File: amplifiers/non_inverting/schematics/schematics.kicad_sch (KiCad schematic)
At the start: 5 parts, among them J1 15V, U1 LM741

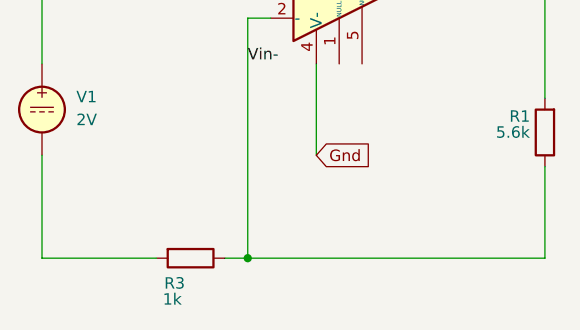
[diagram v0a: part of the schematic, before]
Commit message: docs: reorganize non-inverting amplifier schematics and add documentation
Completes documentation for the non-inverting amplifier circuit using
the LM741 operational amplifier. The schematics have been moved from
the LM741 directory to a dedicated non-inverting amplifier directory.

Only specific measurements for the LM741 will be foubd under the LM741
directory going forward.

Breaking changes: None

Resolves: None
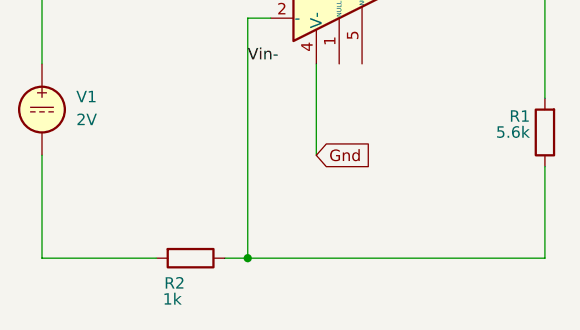
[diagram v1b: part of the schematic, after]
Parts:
- renumbered R3 to R2
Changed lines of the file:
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@@
 		(on_board yes)
 		(dnp no)
-		(property "Reference" "R3"
+		(property "Reference" "R2"
 			(at 35.052 62.484 90)
 			(effects
@@
 			(project "differential_amplifier"
 				(path "/872f1d81-1815-459b-9f9e-3f0909be5d1a"
-					(reference "R3")
+					(reference "R2")
 					(unit 1)
 				)
